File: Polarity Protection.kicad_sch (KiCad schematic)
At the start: 5 parts, among them Q201 MCU18P10Y-TP

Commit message: fix: bom improvements & more notes
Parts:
- D201: Notes (none) -> VZ = 10 V, suitable for input over-voltage clamping
- Q201: Notes (none) -> VDS > 100 V, ID > 2 A, P-channel device suitable for high-s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
- TP201: footprint TestPoint:TestPoint_Pad_D1.5mm -> RD-Testpoints:TestPoint_Pad_D1.5mm
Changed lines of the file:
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@@
+			)
+		)
+		(property "Notes" "VZ = 10 V, suitable for input over-voltage clamping"
+			(at 157.48 87.63 0)
+			(effects
+				(font
+					(size 1.27 1.27)
+				)
+				(hide yes)
 			)
 		)
@@
 			)
 		)
+		(property "Notes" "VDS > 100 V, ID > 2 A, P-channel device suitable for high-side switching"
+			(at 149.86 73.66 0)
+			(effects
+				(font
+					(size 1.27 1.27)
+				)
+				(hide yes)
+			)
+		)
 		(pin "1"
 		)
@@
 			)
 		)
-		(property "Footprint" "TestPoint:TestPoint_Pad_D1.5mm"
+		(property "Footprint" "RD-Testpoints:TestPoint_Pad_D1.5mm"
 			(at 170.18 59.69 0)
 			(effects

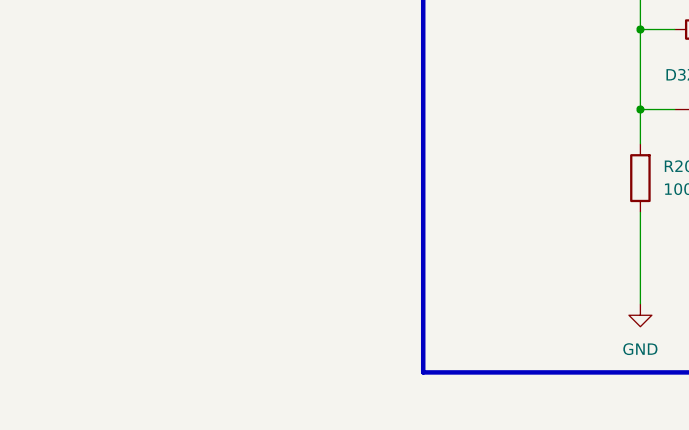
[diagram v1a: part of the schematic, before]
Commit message: feat: ERC/DRC checks
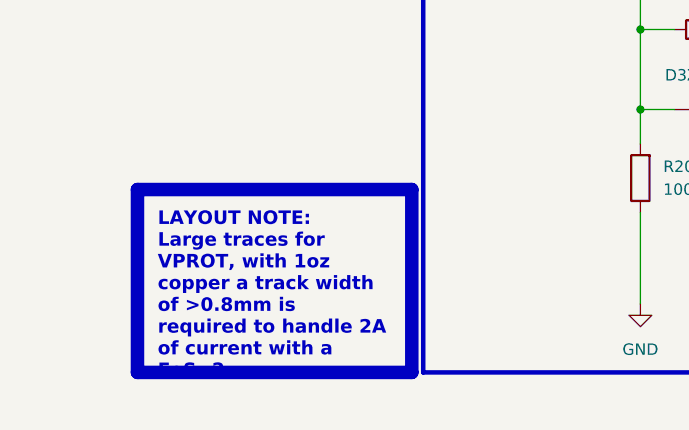
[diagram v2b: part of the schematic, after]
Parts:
- R201, R202: Manufacturer (none) -> Analog Technologies

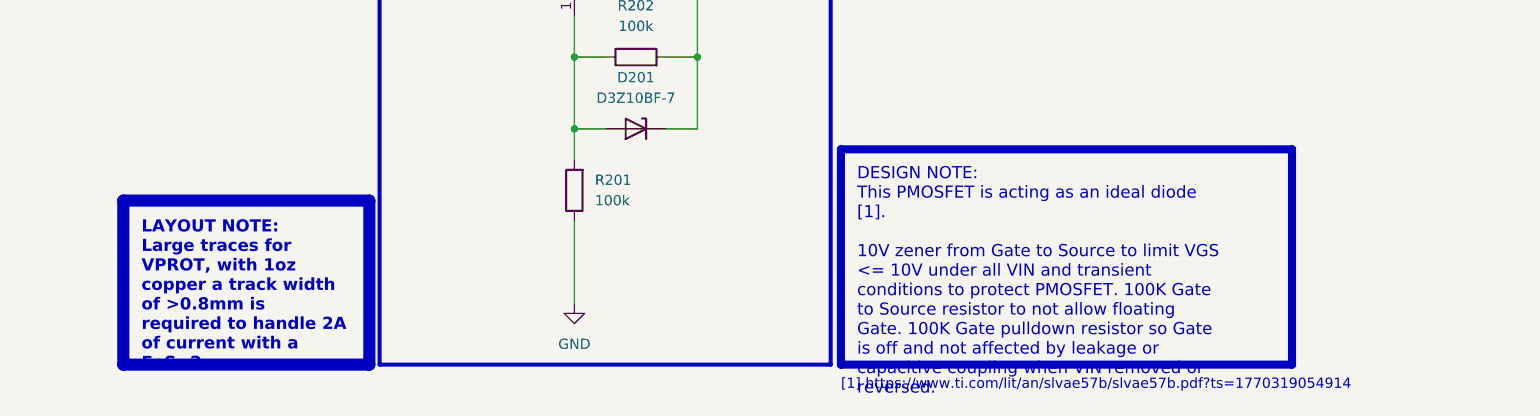
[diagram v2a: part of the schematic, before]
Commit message: feat!: added OC protection, redesigned board from near scratch, size increase
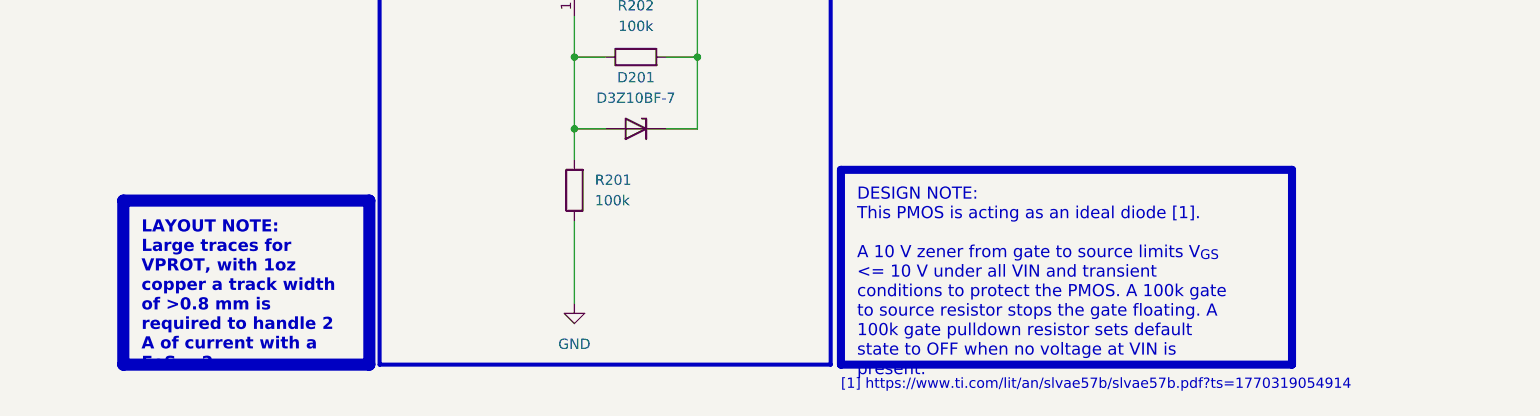
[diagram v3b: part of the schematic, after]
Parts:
- TP201: footprint RD-Testpoints:TestPoint_Pad_D1.5mm -> RD-Testpoints:TestPoint_Pad_D1.0mm
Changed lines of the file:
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@@
 		)
 	)
-	(text_box "DESIGN NOTE:\nThis PMOSFET is acting as an ideal diode [1].\n\n10V zener from Gate to Source to limit VGS <= 10V under all VIN and transient conditions to protect PMOSFET. 100K Gate to Source resistor to not allow floating Gate. 100K Gate pulldown resistor so Gate is off and not affected by leakage or capacitive coupling when VIN removed or reversed."
+	(text_box "DESIGN NOTE:\nThis PMOS is acting as an ideal diode [1].\n\nA 10 V zener from gate to source limits V_{GS} <= 10 V under all VIN and transient conditions to protect the PMOS. A 100k gate to source resistor stops the gate floating. A 100k gate pulldown resistor sets default state to OFF when no voltage at VIN is present."
 		(exclude_from_sim no)
-		(at 182.88 90.17 0)
-		(size 55.88 26.67)
+		(at 182.88 92.71 0)
+		(size 55.88 24.13)
 		(margins 2 2 2 2)
 		(stroke
@@
 		)
 	)
-	(text_box "LAYOUT NOTE:\nLarge traces for VPROT, with 1oz copper a track width of >0.8mm is required to handle 2A of current with a FoS=2."
+	(text_box "LAYOUT NOTE:\nLarge traces for VPROT, with 1oz copper a track width of >0.8 mm is required to handle 2 A of current with a FoS = 2."
 		(exclude_from_sim no)
 		(at 93.98 96.52 0)
@@
 			)
 		)
-		(property "Footprint" "RD-Testpoints:TestPoint_Pad_D1.5mm"
+		(property "Footprint" "RD-Testpoints:TestPoint_Pad_D1.0mm"
 			(at 170.18 59.69 0)
 			(effects
